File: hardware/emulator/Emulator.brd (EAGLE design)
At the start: 69.6 x 71 mm, 41 parts, among them T1 ZVP2106ASTZ, T2 2N5401, U1 DEV-16771_REDUCED_PINS, U2 OPA2277PA, U3 MCP4822-E/P, U4 LM6132BIN, U5 L7808ABV, U6 L7908CV

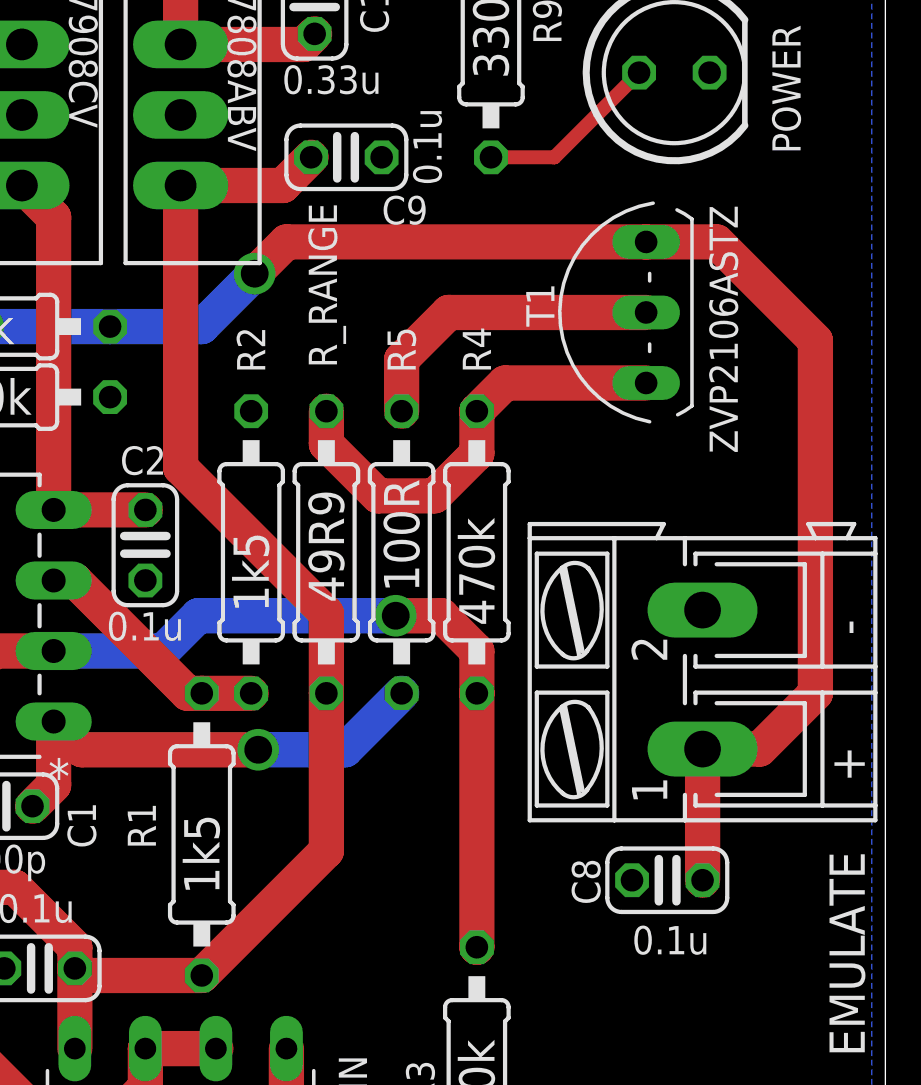
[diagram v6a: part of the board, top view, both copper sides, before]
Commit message: Update the emulation MOSFET device
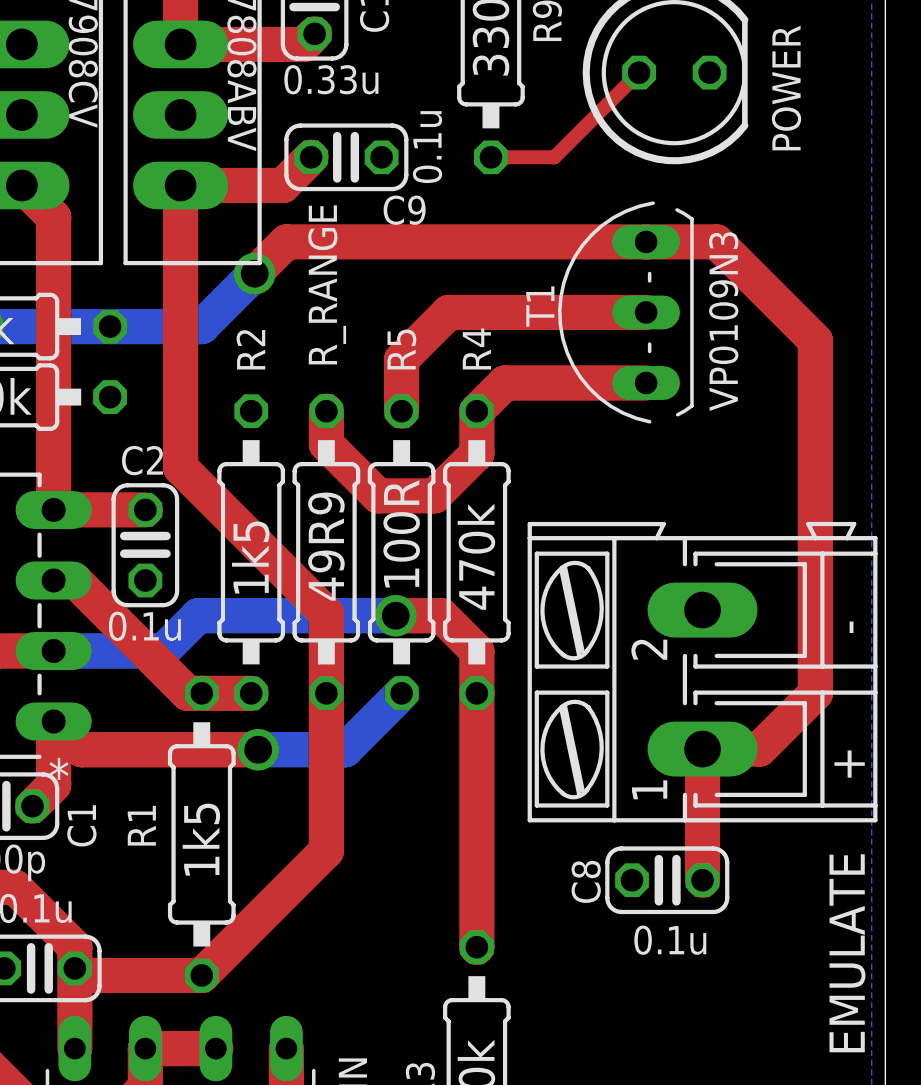
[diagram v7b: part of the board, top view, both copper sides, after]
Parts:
- T1: value ZVP2106ASTZ -> VP0109N3
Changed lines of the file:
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@@
 <attribute name="POPULARITY" value="81" x="63.246" y="40.64" size="1.778" layer="27" rot="R270" display="off"/>
 <attribute name="SPICEPREFIX" value="R" x="63.246" y="40.64" size="1.778" layer="27" rot="R270" display="off"/>
-<attribute name="VALUE" x="43.815" y="21.5646" size="1.27" layer="25" ratio="10" rot="R270"/>
+<attribute name="VALUE" x="43.815" y="22.0726" size="1.27" layer="25" ratio="10" rot="R270"/>
 </element>
 <element name="R2" library="rcl" library_urn="urn:adsk.eagle:library:334" package="0207/10" package3d_urn="urn:adsk.eagle:package:23491/2" value="1k5" x="46.228" y="30.988" smashed="yes" rot="R270">
@@
 <attribute name="POPULARITY" value="81" x="60.452" y="62.484" size="1.778" layer="27" rot="R270" display="off"/>
 <attribute name="SPICEPREFIX" value="R" x="60.452" y="62.484" size="1.778" layer="27" rot="R270" display="off"/>
-<attribute name="VALUE" x="45.593" y="31.7246" size="1.27" layer="25" ratio="10" rot="R270"/>
+<attribute name="VALUE" x="45.593" y="32.2326" size="1.27" layer="25" ratio="10" rot="R270"/>
 </element>
 <element name="R3" library="rcl" library_urn="urn:adsk.eagle:library:334" package="0207/10" package3d_urn="urn:adsk.eagle:package:23491/2" value="470k" x="54.356" y="11.684" smashed="yes" rot="R270">
@@
 <attribute name="POPULARITY" value="81" x="64.00799375" y="62.484" size="1.778" layer="27" rot="R270" display="off"/>
 <attribute name="SPICEPREFIX" value="R" x="64.00799375" y="62.484" size="1.778" layer="27" rot="R270" display="off"/>
-<attribute name="VALUE" x="53.72099375" y="32.2326" size="1.27" layer="25" ratio="10" rot="R270"/>
+<attribute name="VALUE" x="53.72099375" y="32.7406" size="1.27" layer="25" ratio="10" rot="R270"/>
 </element>
 <element name="R_RANGE" library="rcl" library_urn="urn:adsk.eagle:library:334" package="0207/10" package3d_urn="urn:adsk.eagle:package:23491/2" value="49R9" x="48.93733125" y="30.988" smashed="yes" rot="R270">
@@
 <attribute name="VALUE" x="51.0116625" y="33.6296" size="1.27" layer="25" ratio="10" rot="R270"/>
 </element>
-<element name="T1" library="ZVP2106A" package="TO92-SGD" value="ZVP2106ASTZ" x="60.452" y="39.624" smashed="yes" rot="R90">
+<element name="T1" library="ZVP2106A" package="TO92-SGD" value="VP0109N3" x="60.452" y="39.624" smashed="yes" rot="R90">
 <attribute name="NAME" x="57.15" y="39.116" size="1.016" layer="25" ratio="10" rot="R90"/>
-<attribute name="VALUE" x="63.754" y="34.544" size="1.016" layer="25" ratio="10" rot="R90"/>
+<attribute name="VALUE" x="63.754" y="36.068" size="1.016" layer="25" ratio="10" rot="R90"/>
 </element>
 <element name="T2" library="transistor-neu-to92" package="TO92-EBC" package3d_urn="urn:adsk.eagle:package:28763/2" value="2N5401" x="27.432" y="48.768" smashed="yes" rot="R180">

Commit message: Update board version
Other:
- board text added: "SOCRAETES Emulator v0.3.11 Universität Duisburg-Essen - NES Hochschule Niederrhein - FB 03"
- board text removed: "SOCRAETES Emulator v0.2.8 Universität Duisburg-Essen - NES Hochschule Niederrhein - FB 03"
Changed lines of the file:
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@@
 <wire x1="69.068" y1="71.044" x2="-0.508" y2="71.044" width="0" layer="20"/>
 <wire x1="-0.508" y1="71.044" x2="-0.508" y2="0" width="0" layer="20"/>
-<text x="64.516" y="70.104" size="1.016" layer="25" rot="R180">SOCRAETES Emulator v0.2.8
+<text x="64.516" y="70.104" size="1.016" layer="25" rot="R180">SOCRAETES Emulator v0.3.11
 Universität Duisburg-Essen - NES
 Hochschule Niederrhein - FB 03</text>
